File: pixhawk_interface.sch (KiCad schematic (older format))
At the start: 15 parts, among them J5 DF13-6

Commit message: Continued syncing with original design.
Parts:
- removed F? (x7): FUSE, littelfuse-1206, symbol FUSE
- added F2, F3, F4, F5, F6, F7, F8: 4A 5V, littelfuse-1206, symbol FUSE
- F1: renamed from F?; value FUSE -> 4A 5V; Digikey (none) -> F5786CT-ND
- F10, F28: renamed from F?; value FUSE -> 1.1A 5V; Digikey (none) -> F3366CT-ND
- J3: renamed from P?; footprint (none) -> ~; Digikey (none) -> H3436-ND
- J4: renamed from P?; footprint (none) -> ~; Digikey (none) -> H3435-ND
- J5: footprint (none) -> ~; Digikey (none) -> H3436-ND
- gave numbers to parts that had none: 2
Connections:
- wire segments 160 -> 113
- no-connect marks 1 -> 2

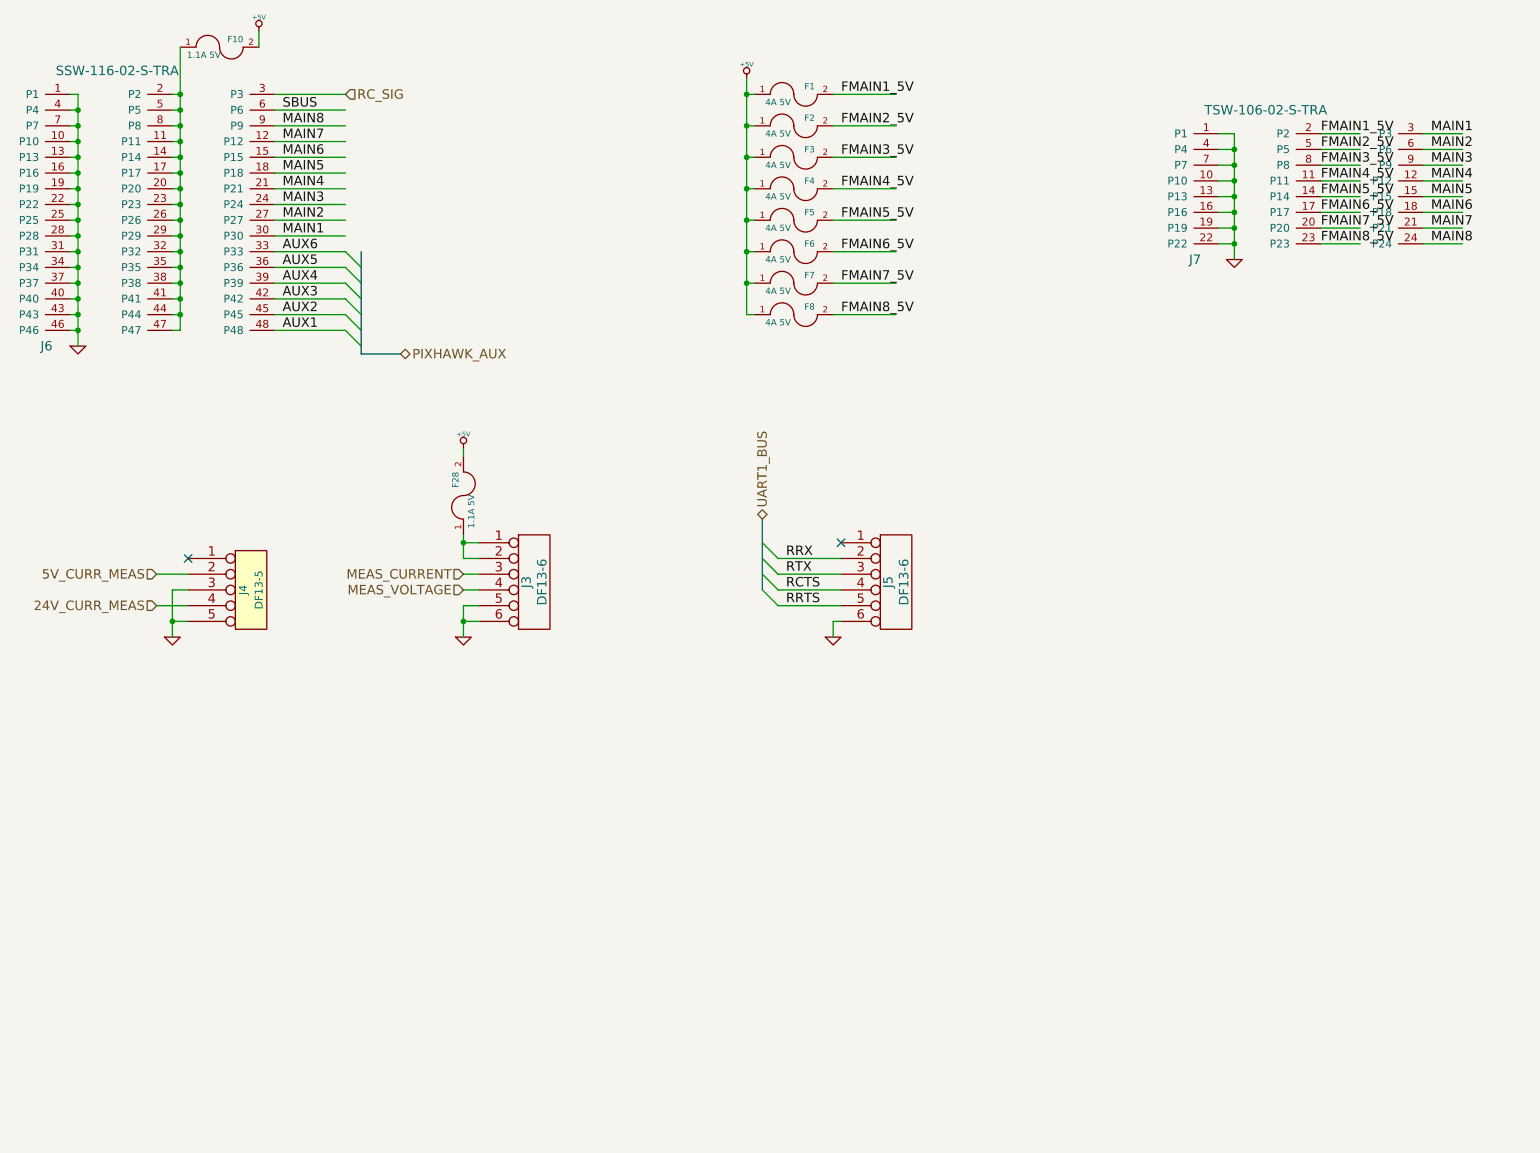
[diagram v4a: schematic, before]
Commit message: Updating design with new 12v bus.
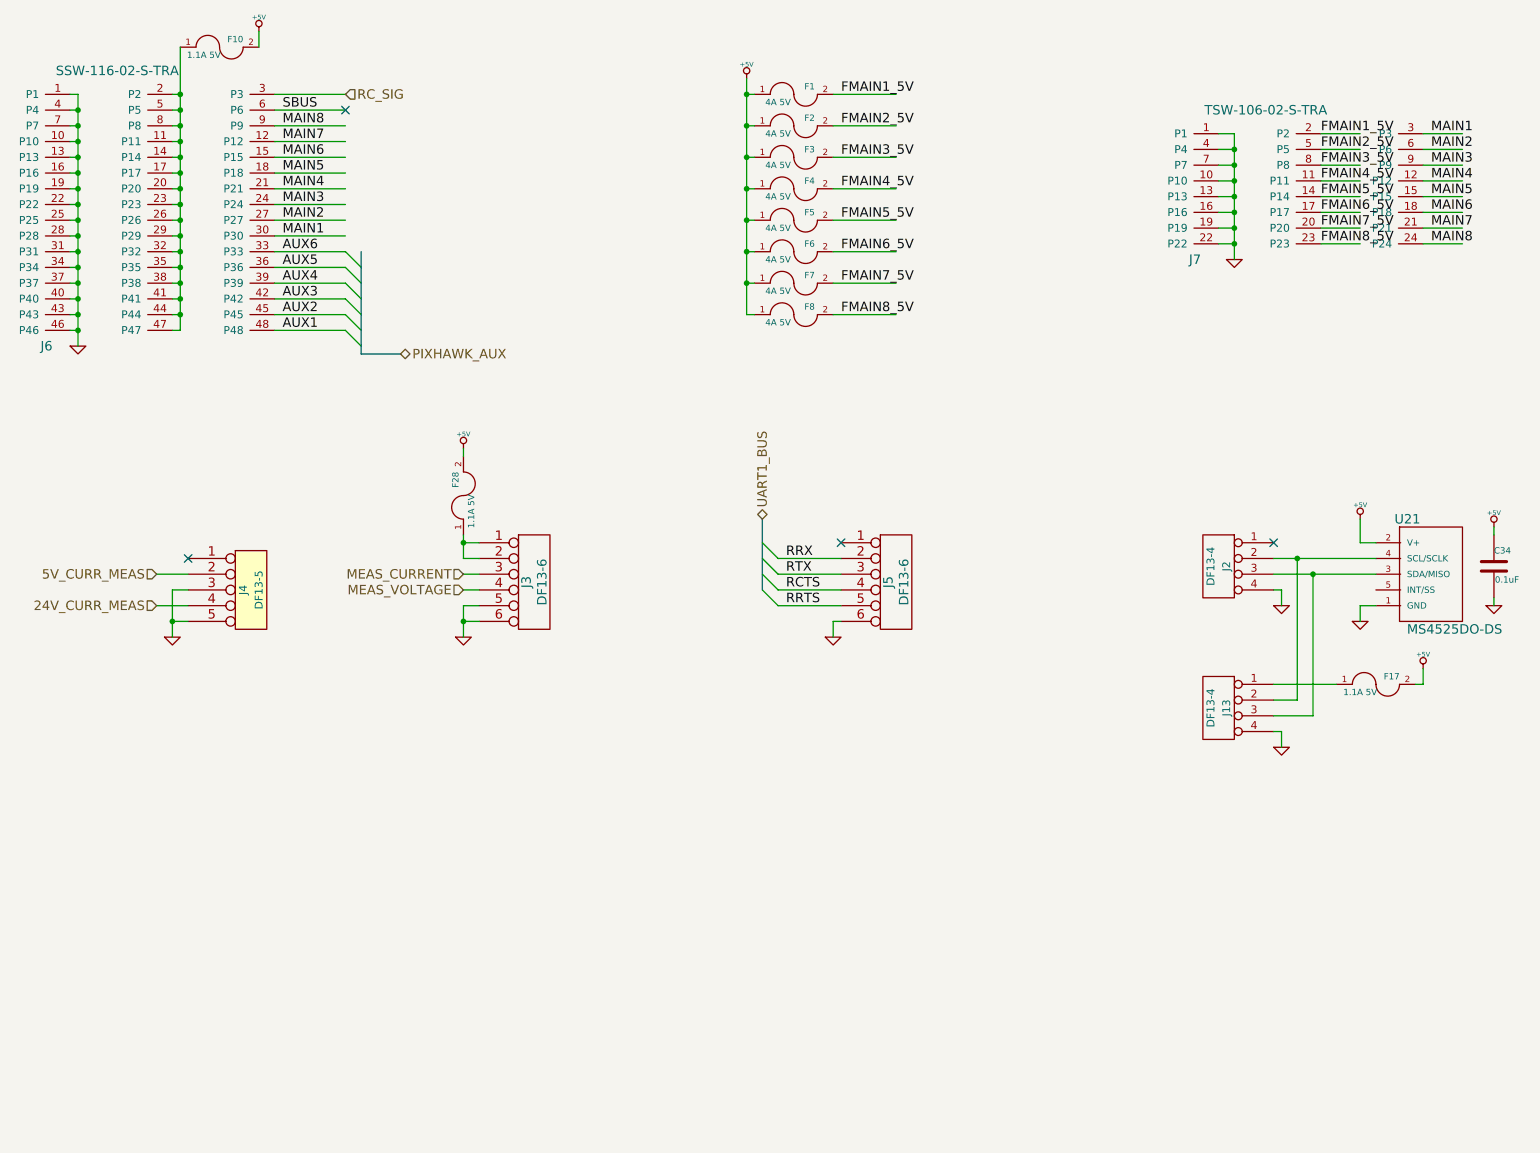
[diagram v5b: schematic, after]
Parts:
- added C34: 0.1uF, SM0805, symbol C
- added F17: 1.1A 5V, littelfuse-1206, symbol FUSE
- added J13, J2: DF13-4, ~, symbol CONN_4
- added U21: MS4525DO-DS, ~, symbol MS4525DO-DS
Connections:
- wire segments 113 -> 132
- no-connect marks 2 -> 4
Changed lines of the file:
@@
 LIBS:w_transistor
 LIBS:w_analog
+LIBS:p_meas_spec
 LIBS:distro-cache
 EELAYER 27 0
@@
 $EndComp
 $Comp
-L GND #PWR041
+L GND #PWR046
 U 1 1 55CD066E
 P 8450 2100
-F 0 "#PWR041" H 8450 2100 30  0001 C CNN
+F 0 "#PWR046" H 8450 2100 30  0001 C CNN
 F 1 "GND" H 8450 2030 30  0001 C CNN
 F 2 "" H 8450 2100 60  0000 C CNN
@@
 FMAIN8_5V
 $Comp
-L +5V #PWR042
+L +5V #PWR047
 U 1 1 55CD06A4
 P 5350 950
-F 0 "#PWR042" H 5350 1040 20  0001 C CNN
+F 0 "#PWR047" H 5350 1040 20  0001 C CNN
 F 1 "+5V" H 5350 1040 30  0000 C CNN
 F 2 "" H 5350 950 60  0000 C CNN
@@
 FMAIN8_5V
 $Comp
-L GND #PWR043
+L GND #PWR048
 U 1 1 55CD06FA
 P 1100 2650
-F 0 "#PWR043" H 1100 2650 30  0001 C CNN
+F 0 "#PWR048" H 1100 2650 30  0001 C CNN
 F 1 "GND" H 1100 2580 30  0001 C CNN
 F 2 "" H 1100 2650 60  0000 C CNN
@@
 $EndComp
 $Comp
-L +5V #PWR044
+L +5V #PWR049
 U 1 1 55CD0706
 P 2250 650
-F 0 "#PWR044" H 2250 740 20  0001 C CNN
+F 0 "#PWR049" H 2250 740 20  0001 C CNN
 F 1 "+5V" H 2250 740 30  0000 C CNN
 F 2 "" H 2250 650 60  0000 C CNN
@@
 	5550 4300 5950 4300
 $Comp
-L GND #PWR045
+L GND #PWR050
 U 1 1 55CD380E
 P 5900 4500
-F 0 "#PWR045" H 5900 4500 30  0001 C CNN
+F 0 "#PWR050" H 5900 4500 30  0001 C CNN
 F 1 "GND" H 5900 4430 30  0001 C CNN
 F 2 "" H 5900 4500 60  0000 C CNN
@@
 AUX1
 $Comp
-L +5V #PWR046
+L +5V #PWR051
 U 1 1 55CD4137
 P 3550 3300
-F 0 "#PWR046" H 3550 3390 20  0001 C CNN
+F 0 "#PWR051" H 3550 3390 20  0001 C CNN
 F 1 "+5V" H 3550 3390 30  0000 C CNN
 F 2 "" H 3550 3300 60  0000 C CNN
@@
 	3550 3900 3650 3900
 $Comp
-L GND #PWR047
+L GND #PWR052
 U 1 1 55CD42B3
 P 3550 4500
-F 0 "#PWR047" H 3550 4500 30  0001 C CNN
+F 0 "#PWR052" H 3550 4500 30  0001 C CNN
 F 1 "GND" H 3550 4430 30  0001 C CNN
 F 2 "" H 3550 4500 60  0000 C CNN
@@
 	1800 4300 1600 4300
 $Comp
-L GND #PWR048
+L GND #PWR053
 U 1 1 55CD489A
 P 1700 4500
-F 0 "#PWR048" H 1700 4500 30  0001 C CNN
+F 0 "#PWR053" H 1700 4500 30  0001 C CNN
 F 1 "GND" H 1700 4430 30  0001 C CNN
 F 2 "" H 1700 4500 60  0000 C CNN
@@
 $EndComp
 NoConn ~ 5950 3900
+NoConn ~ 2800 1150
+$Comp
+L MS4525DO-DS U21
+U 1 1 55D8FAEE
+P 9600 4150
+F 0 "U21" H 9550 4550 60  0000 C CNN
+F 1 "MS4525DO-DS" H 9850 3850 60  0000 C CNN
+F 2 "~" H 9600 4150 60  0000 C CNN
+F 3 "~" H 9600 4150 60  0000 C CNN
+F 4 "223-1110-ND" H 9600 4150 60  0001 C CNN "Digikey"
+	1    9600 4150
+	1    0    0    -1
+$EndComp
+$Comp
+L +5V #PWR054
+U 1 1 55D8FAFB
+P 9250 3750
+F 0 "#PWR054" H 9250 3840 20  0001 C CNN
+F 1 "+5V" H 9250 3840 30  0000 C CNN
+F 2 "" H 9250 3750 60  0000 C CNN
+F 3 "" H 9250 3750 60  0000 C CNN
+	1    9250 3750
+	1    0    0    -1
+$EndComp
+Wire Wire Line
+	9350 3900 9250 3900
+Wire Wire Line
+	9250 3900 9250 3750
+$Comp
+L GND #PWR055
+U 1 1 55D8FBA5
+P 9250 4400
+F 0 "#PWR055" H 9250 4400 30  0001 C CNN
+F 1 "GND" H 9250 4330 30  0001 C CNN
+F 2 "" H 9250 4400 60  0000 C CNN
+F 3 "" H 9250 4400 60  0000 C CNN
+	1    9250 4400
+	1    0    0    -1
+$EndComp
+Wire Wire Line
+	9350 4300 9250 4300
+Wire Wire Line
+	9250 4300 9250 4400
+$Comp
+L CONN_4 J2
+U 1 1 55D8FC53
+P 8350 4050
+F 0 "J2" V 8300 4050 50  0000 C CNN
+F 1 "DF13-4" V 8400 4050 50  0000 C CNN
+F 2 "~" H 8350 4050 60  0000 C CNN
+F 3 "~" H 8350 4050 60  0000 C CNN
+F 4 "H3434-ND" V 8350 4050 60  0001 C CNN "Digikey"
+	1    8350 4050
+	-1   0    0    -1
+$EndComp
+Wire Wire Line
+	8700 4000 9350 4000
+Wire Wire Line
+	8700 4100 9350 4100
+$Comp
+L GND #PWR056
+U 1 1 55D8FE86
+P 8750 4300
+F 0 "#PWR056" H 8750 4300 30  0001 C CNN
+F 1 "GND" H 8750 4230 30  0001 C CNN
+F 2 "" H 8750 4300 60  0000 C CNN
+F 3 "" H 8750 4300 60  0000 C CNN
+	1    8750 4300
+	1    0    0    -1
+$EndComp
+Wire Wire Line
+	8750 4300 8750 4200
+Wire Wire Line
+	8750 4200 8700 4200
+NoConn ~ 8700 3900
+$Comp
+L CONN_4 J13
+U 1 1 55D901C5
+P 8350 4950
+F 0 "J13" V 8300 4950 50  0000 C CNN
+F 1 "DF13-4" V 8400 4950 50  0000 C CNN
+F 2 "~" H 8350 4950 60  0000 C CNN
+F 3 "~" H 8350 4950 60  0000 C CNN
+F 4 "H3434-ND" V 8350 4950 60  0001 C CNN "Digikey"
+	1    8350 4950
+	-1   0    0    -1
+$EndComp
+$Comp
+L C C34
+U 1 1 55D902B6
+P 10100 4050
+F 0 "C34" H 10100 4150 40  0000 L CNN
+F 1 "0.1uF" H 10106 3965 40  0000 L CNN
+F 2 "SM0805" H 10138 3900 30  0001 C CNN
+F 3 "~" H 10100 4050 60  0000 C CNN
+F 4 "399-11163-1-ND" H 10100 4050 60  0001 C CNN "Digikey"
+	1    10100 4050
+	1    0    0    -1
+$EndComp
+$Comp
+L +5V #PWR057
+U 1 1 55D902BC
+P 10100 3800
+F 0 "#PWR057" H 10100 3890 20  0001 C CNN
+F 1 "+5V" H 10100 3890 30  0000 C CNN
+F 2 "" H 10100 3800 60  0000 C CNN
+F 3 "" H 10100 3800 60  0000 C CNN
+	1    10100 3800
+	1    0    0    -1
+$EndComp
+$Comp
+L GND #PWR058
+U 1 1 55D902C2
+P 10100 4300
+F 0 "#PWR058" H 10100 4300 30  0001 C CNN
+F 1 "GND" H 10100 4230 30  0001 C CNN
+F 2 "" H 10100 4300 60  0000 C CNN
+F 3 "" H 10100 4300 60  0000 C CNN
+	1    10100 4300
+	1    0    0    -1
+$EndComp
+Wire Wire Line
+	10100 4300 10100 4250
+Wire Wire Line
+	10100 3850 10100 3800
+$Comp
+L FUSE F17
+U 1 1 55D902D7
+P 9350 4800
+F 0 "F17" H 9450 4850 40  0000 C CNN
+F 1 "1.1A 5V" H 9250 4750 40  0000 C CNN
+F 2 "littelfuse-1206" H 9350 4800 60  0001 C CNN
+F 3 "~" H 9350 4800 60  0000 C CNN
+F 4 "F3366CT-ND" H 9350 4800 60  0001 C CNN "Digikey"
+	1    9350 4800
+	1    0    0    -1
+$EndComp
+$Comp
+L +5V #PWR059
+U 1 1 55D902DD
+P 9650 4700
+F 0 "#PWR059" H 9650 4790 20  0001 C CNN
+F 1 "+5V" H 9650 4790 30  0000 C CNN
+F 2 "" H 9650 4700 60  0000 C CNN
+F 3 "" H 9650 4700 60  0000 C CNN
+	1    9650 4700
+	1    0    0    -1
+$EndComp
+Wire Wire Line
+	9600 4800 9650 4800
+Wire Wire Line
+	9650 4800 9650 4700
+Wire Wire Line
+	9100 4800 8700 4800
+$Comp
+L GND #PWR060
+U 1 1 55D90441
+P 8750 5200
+F 0 "#PWR060" H 8750 5200 30  0001 C CNN
+F 1 "GND" H 8750 5130 30  0001 C CNN
+F 2 "" H 8750 5200 60  0000 C CNN
+F 3 "" H 8750 5200 60  0000 C CNN
+	1    8750 5200
+	1    0    0    -1
+$EndComp
+Wire Wire Line
+	8700 5100 8750 5100
+Wire Wire Line
+	8750 5100 8750 5200
+Wire Wire Line
+	8700 4900 8850 4900
+Wire Wire Line
+	8850 4900 8850 4000
+Connection ~ 8850 4000
+Wire Wire Line
+	8700 5000 8950 5000
+Wire Wire Line
+	8950 5000 8950 4100
+Connection ~ 8950 4100
 $EndSCHEMATC

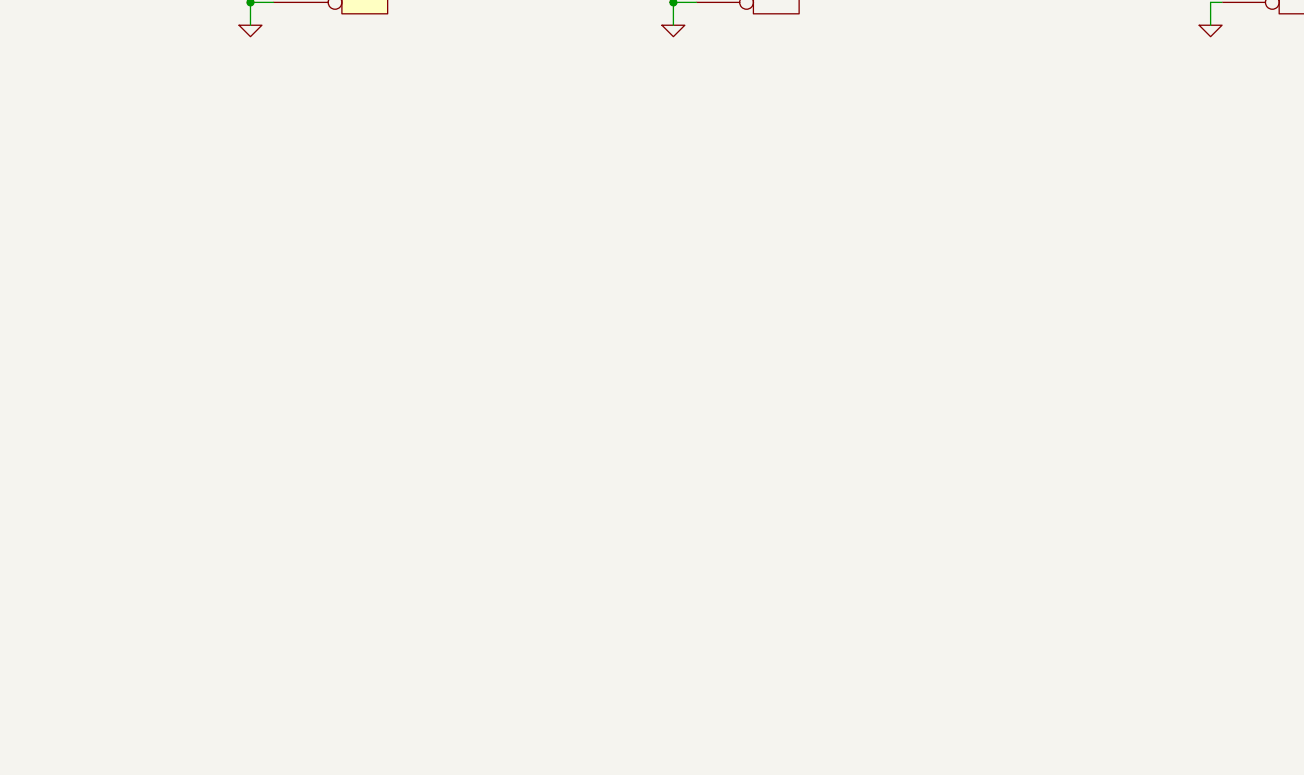
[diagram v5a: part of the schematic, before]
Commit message: Adding gps receiver, updating netlist and completing component assignment.
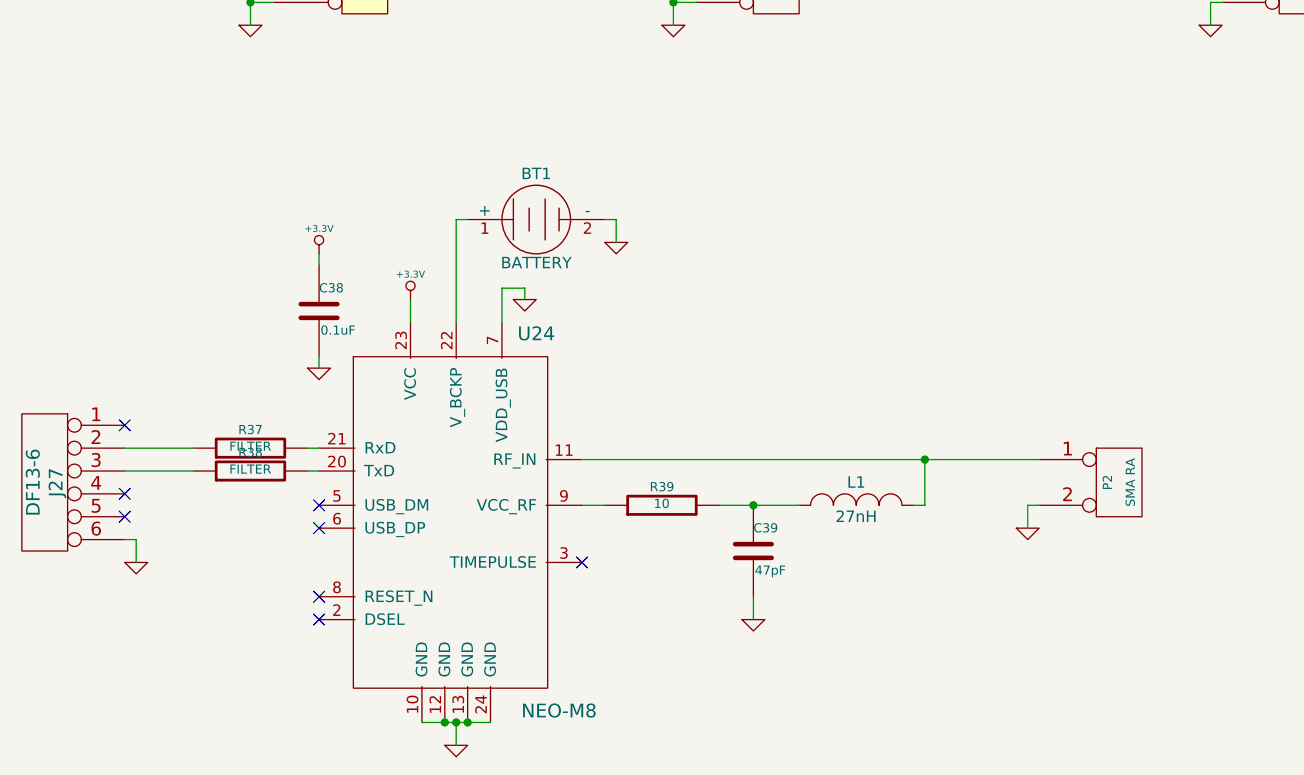
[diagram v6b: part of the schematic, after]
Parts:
- added BT1: BATTERY, ~, symbol BATTERY
- added C38: 0.1uF, SM0805, symbol C
- added C39: 47pF, ~, symbol C
- added J27: DF13-6, ~, symbol CONN_6
- added L1: 27nH, ~, symbol INDUCTOR_SMALL
- added P2: SMA RA, ~, symbol CONN_2
- added R37, R38: FILTER, ~, symbol R
- added R39: 10, ~, symbol R
- added U24: NEO-M8, ~, symbol NEO-M8
- F5: value 4A 5V -> 4A 5V
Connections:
- net labels added: +3.3V
- wire segments 132 -> 158
- no-connect marks 4 -> 12

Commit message: Preliminary layout complete.
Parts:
- J7: value TSW-106-02-S-TRA -> TSW-108-08-G-T-RA; footprint con-samtec-TSW-106-02-S-T-RA -> ~
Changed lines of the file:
@@
 LIBS:p_ti
 LIBS:p_switch
-LIBS:w_connectors
 LIBS:p_micrel
 LIBS:p_samtec
-LIBS:w_transistor
-LIBS:w_analog
 LIBS:p_meas_spec
 LIBS:p_ublox
@@
 Sheet 4 9
 Title ""
-Date "25 aug 2015"
+Date "27 aug 2015"
 Rev ""
 Comp ""
@@
 P 8850 1650
 F 0 "J7" H 8200 1200 60  0000 C CNN
-F 1 "TSW-106-02-S-TRA" H 8650 2150 60  0000 C CNN
-F 2 "con-samtec-TSW-106-02-S-T-RA" H 9500 1300 60  0001 C CNN
+F 1 "TSW-108-08-G-T-RA" H 8650 2150 60  0000 C CNN
+F 2 "~" H 9500 1300 60  0001 C CNN
 F 3 "~" H 9500 1300 60  0000 C CNN
 	1    8850 1650
